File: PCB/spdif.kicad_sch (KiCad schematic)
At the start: 22 parts, among them U17 PLR237/T10BK, U7 DIR9001PWR, Y1 24.576MHz

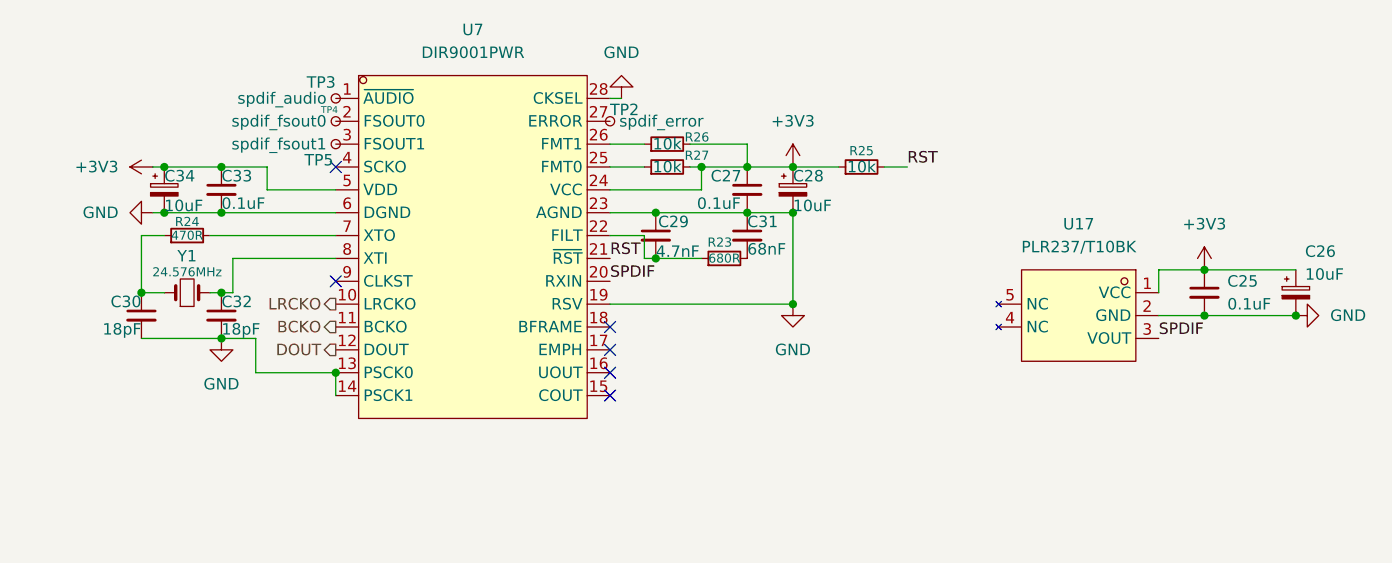
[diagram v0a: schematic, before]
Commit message: updated schematics
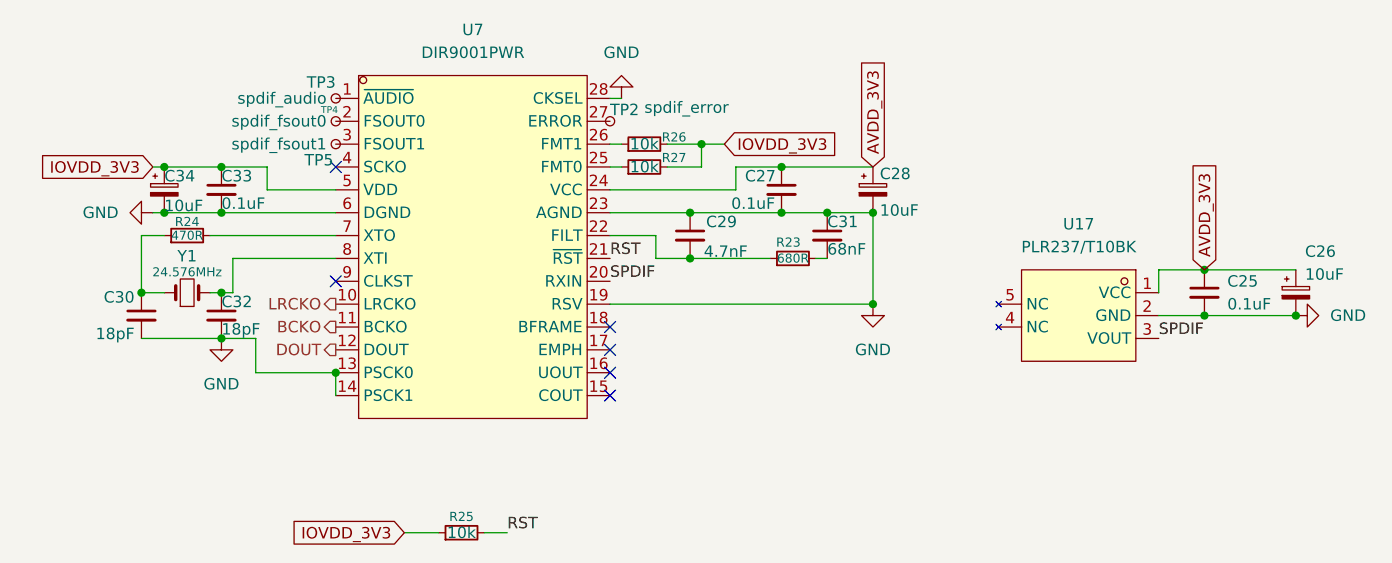
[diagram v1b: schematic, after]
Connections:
- net +3V3 renamed AVDD_3V3
- net AVDD_3V3: no longer C33.1, C34.1, R25.1, R26.2, R27.2, U7.5 (VDD)
- new net IOVDD_3V3: C33.1, C34.1, R25.1, R26.2, R27.2, U7.5 (VDD)
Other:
- moved on the sheet: C27, C28, C29, C31, R23, R25, R26, R27
